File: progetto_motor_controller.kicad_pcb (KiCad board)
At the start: 4 copper layers, 55 parts, among them J1 USB_B_Micro, J2 Screw_Terminal_01x02, J3 SWD, J4 Screw_Terminal_01x03, Q1 AO3401A, SW1 SW_SPDT, U1 STM32F103C8Tx, U2 LMR504010-Q1, U3 USBLC6-2P6, U4 L6234PD, U5 INA240A2D, U6 INA240A2D, Y1 16MHz

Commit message: Third commit
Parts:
- removed C10: 10n, Capacitor_SMD:C_0402_1005Metric
- removed C11: 100 nF, Capacitor_SMD:C_0603_1608Metric
- removed C12: 10 uF, Capacitor_SMD:C_1206_3216Metric
- removed C13, C15: 0.1uF, Capacitor_SMD:C_0402_1005Metric
- removed C14: 220nF, Capacitor_SMD:C_0402_1005Metric
- removed C18: 100nF, Capacitor_SMD:C_0603_1608Metric
- removed C19: 100uF, Capacitor_SMD:CP_Elec_6.3x5.8
- removed D4, D5: IN4148, Diode_SMD:D_SOD-323F
- removed F1: 500mA, Fuse:Fuse_0603_1608Metric
- removed J2: Screw_Terminal_01x02, TerminalBlock_Phoenix:TerminalBlock_Phoenix_PT-1,5-2-3.5-H_1x02_P3.50mm_Horizontal
- removed J3: SWD, Connector_PinSocket_1.27mm:PinSocket_2x05_P1.27mm_Vertical_SMD
- removed L1: 39n, Inductor_SMD:L_0402_1005Metric
- removed L2: 10 uH, Inductor_SMD:L_Sunlord_MWSA0518_5.4x5.2mm
- removed Q1: AO3401A, Package_TO_SOT_SMD:SOT-23
- removed R10, R9: 2m, Resistor_SMD:R_Shunt_Ohmite_LVK12
- removed U5, U6: INA240A2D, Package_SO:TSSOP-8_4.4x3mm_P0.65mm
- added J8: Screw_Terminal_01x02, TerminalBlock_Phoenix:TerminalBlock_Phoenix_PT-1,5-2-3.5-H_1x02_P3.50mm_Horizontal, F.Cu at (175.5, 98.9)
- added Q8: AO3401A, Package_TO_SOT_SMD:SOT-23, F.Cu at (184.2, 97.0)
- added U7: MYRGC07506_1, MyLibrary:Murata_picoBK, F.Cu at (133.2, 66.4)
- added U8: TLV707, MyLibrary:TLV707, F.Cu at (157.6, 90.3)
- C16: value 10nF -> 0.1uF; moved to F.Cu
- C17: value 1uF -> 0.1uF; footprint Capacitor_SMD:C_0603_1608Metric -> Capacitor_SMD:C_0402_1005Metric; moved to F.Cu
- C6: value 10u -> 100n; footprint Capacitor_SMD:C_1206_3216Metric -> Capacitor_SMD:C_0402_1005Metric
- C8: value 1u -> 2u2
- D1, D3: value B5819W -> LED_Small; footprint Diode_SMD:D_SOD-123 -> LED_SMD:LED_0603_1608Metric
- J4: moved to F.Cu
- R5: value 100k -> 1k5
- R6: value 33k -> 1k5
- R7: footprint Resistor_SMD:R_0603_1608Metric -> Resistor_SMD:R_0402_1005Metric
- R8: value 4.7K -> 10k; moved to F.Cu
- U1: value STM32F103C8Tx -> STM32F303RETx; footprint Package_QFP:LQFP-48_7x7mm_P0.5mm -> Package_QFP:LQFP-64_10x10mm_P0.5mm
- U2: value LMR504010-Q1 -> SN65HVD253D; footprint Package_TO_SOT_SMD:TSOT-23-6_HandSoldering -> Package_SO:SOIC-8_3.9x4.9mm_P1.27mm
- U4: value L6234PD -> TMC6140; footprint Package_TO_SOT_SMD:L6234PD -> MyLibrary:TMC6140-LA; moved to F.Cu
- moved J4 58.3 mm to (124.9, 118.2), turned to 0 degrees
- moved U2 57.1 mm to (102.4, 78.6), turned to 0 degrees
- moved C17 48.1 mm to (174.2, 79.3), turned to 0 degrees
- moved C16 45.4 mm to (174.2, 81.2), turned to 0 degrees
- moved U4 41.3 mm to (107.8, 112.0), turned to 180 degrees
- moved D2 38.1 mm to (163.2, 64.4), turned to 0 degrees
- moved C5 36.8 mm to (112.6, 95.6), turned to 0 degrees
- moved U3 36.4 mm to (119.1, 78.0)
- moved J1 35.2 mm to (119.1, 72.7)
- moved H2 34.4 mm to (134.1, 94.4)
- moved SW1 33.9 mm to (156.8, 81.3), turned to 0 degrees
- moved H4 33.4 mm to (144.2, 93.5)
- moved R4 31.7 mm to (132.3, 108.1), turned to 0 degrees
- moved R3 30.4 mm to (158.6, 67.3)
- moved Y1 30.1 mm to (154.5, 65.3), turned to 0 degrees
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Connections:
- net Net-(U1-Pad16) renamed BOARD_TEMP
- net Net-(U1-Pad38) renamed ENC_B
- C1 pad 1: +3V3 -> 3V3_MCU
- C16 pad 1: Net-(C16-Pad1) -> 3V3_VDAA
- C16 pad 2: Net-(C16-Pad2) -> GND
- C17 pad 1: Net-(C17-Pad1) -> 3V3_VDAA
- C2 pad 1: +3V3 -> 3V3_MCU
- C3 pad 1: +3V3 -> 3V3_MCU
- C4 pad 1: +3V3 -> 3V3_MCU
- C5 pad 1: +3V3 -> 3V3_MCU
- C6 pad 1: BUCK_IN -> 3V3_MCU
- C8 pad 1: +3.3VA -> 5V
- D1 pad 2: +5V -> LED_R
- D2 pad 2: LED_STATUS -> LED_G
- D3 pad 1: BUCK_SW -> Net-(D3-Pad1)
- D3 pad 2: GND -> LED_B
- FB1 pad 1: BUCK_IN -> VDD
- FB1 pad 2: Net-(D1-Pad1) -> Net-(FB1-Pad2)
- J1 pad 1: +5V -> 5V
- J1 pad 4: Net-(J1-Pad4) -> unconnected-(J1-Pad4)
- J1 pad 6: Net-(J1-Pad6) -> unconnected-(J1-Pad6)
- R2 pad 1: Net-(D2-Pad1) -> Net-(D1-Pad1)
- R4 pad 1: Net-(J3-Pad2) -> SWDIO
- R4 pad 2: SWDIO -> Net-(J2-Pad4)
- R5 pad 1: BUCK_IN -> Net-(D2-Pad1)
- R5 pad 2: BUCK_EN -> GND
- R6 pad 1: +3V3 -> Net-(D3-Pad1)
- R6 pad 2: BUCK_FB -> GND
- R7 pad 1: BUCK_FB -> FAN_PWM
- R7 pad 2: GND -> Net-(Q1-Pad2)
- R8 pad 1: L6234_EN -> GND
- R8 pad 2: GND -> Net-(Q1-Pad2)
- SW1 pad 1: +3V3 -> 3V3_MCU
- U1 pad 1: +3V3 -> 3V3_MCU
- U1 pad 10: C1_SENSE -> PWM_HC
- U1 pad 11: C2_SENSE -> unconnected-(U1-Pad11)
- U1 pad 12: Net-(U1-Pad12) -> GND
- U1 pad 13: Net-(U1-Pad13) -> 3V3_VDAA
- U1 pad 14: Net-(U1-Pad14) -> FAN_PWM
- U1 pad 15: Net-(U1-Pad15) -> unconnected-(U1-Pad15)
- U1 pad 17: Net-(U1-Pad17) -> C1_SENSE
- U1 pad 18: Net-(U1-Pad18) -> GND
- U1 pad 19: Net-(U1-Pad19) -> 3V3_MCU
- U1 pad 2: Net-(U1-Pad2) -> unconnected-(U1-Pad2)
- U1 pad 20: Net-(U1-Pad20) -> C2_SENSE
- U1 pad 21: Net-(U1-Pad21) -> unconnected-(U1-Pad21)
- U1 pad 22: Net-(U1-Pad22) -> unconnected-(U1-Pad22)
- U1 pad 23: GND -> PWM_LA
- U1 pad 24: +3V3 -> unconnected-(U1-Pad24)
- U1 pad 25: Net-(U1-Pad25) -> unconnected-(U1-Pad25)
- U1 pad 26: Net-(U1-Pad26) -> PWM_LB
- U1 pad 27: Net-(U1-Pad27) -> PWM_LC
- U1 pad 28: Net-(U1-Pad28) -> ENABLE
- U1 pad 29: PH_A_PWM -> SH_SET
- U1 pad 3: Net-(U1-Pad3) -> unconnected-(U1-Pad3)
- U1 pad 30: PH_B_PWM -> DIAG
- U1 pad 31: PH_C_PWM -> GND
- U1 pad 32: USB_D- -> 3V3_MCU
- U1 pad 33: USB_D+ -> V_EMF_SENSE_C
- U1 pad 34: SWDIO -> unconnected-(U1-Pad34)
- U1 pad 35: GND -> V_EMF_SENSE_B
- U1 pad 36: +3V3 -> V_EMF_SENSE_A
- U1 pad 37: SWCLK -> ENC_A
- U1 pad 39: SWO -> ENC_I
- U1 pad 4: Net-(U1-Pad4) -> unconnected-(U1-Pad4)
- U1 pad 40: Net-(U1-Pad40) -> LED_R
- U1 pad 41: Net-(U1-Pad41) -> LED_G
- U1 pad 42: Net-(U1-Pad42) -> LED_B
- U1 pad 43: L6234_EN -> unconnected-(U1-Pad43)
- U1 pad 44: BOOT0 -> USB_D-
- U1 pad 45: Net-(U1-Pad45) -> USB_D+
- U1 pad 46: LED_STATUS -> SWDIO
- U1 pad 48: +3V3 -> 3V3_MCU
- U1 pad 8: GND -> PWM_HA
- U1 pad 9: +3.3VA -> PWM_HB
- U2 pad 1: BUCK_BST -> CAN_TX
- U2 pad 3: BUCK_FB -> 5V
- U2 pad 4: BUCK_EN -> CAN_RX
- U2 pad 5: BUCK_IN -> GND
- U2 pad 6: BUCK_SW -> CAN_L
- U3 pad 5: +5V -> 5V
- U4 pad 1: GND -> LC
- U4 pad 10: GND -> Net-(68u1-Pad2)
- U4 pad 11: GND -> VDD
- U4 pad 12: +48V -> Net-(C11-Pad1)
- U4 pad 13: L6234_EN -> PWM_HA
- U4 pad 14: PH_C_PWM -> PWM_LA
- U4 pad 15: PH_C -> PWM_HB
- U4 pad 16: Net-(C17-Pad1) -> PWM_LB
- U4 pad 17: Net-(C16-Pad2) -> PWM_HC
- U4 pad 18: Net-(C14-Pad1) -> PWM_LC
- U4 pad 19: GND -> SH_SET
- U4 pad 2: GND -> Net-(C14-Pad2)
- U4 pad 20: GND -> DIAG
- U4 pad 3: L6234_EN -> HB
- U4 pad 4: PH_B_PWM -> PH_B_CS
- U4 pad 5: PH_B_CS -> LB
- U4 pad 6: PH_A_CS -> LA
- U4 pad 7: PH_A_PWM -> PH_A_CS
- U4 pad 8: L6234_EN -> HA
- U4 pad 9: +48V -> Net-(C13-Pad2)
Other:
- copper layers 4 -> 2
- net class Default removed

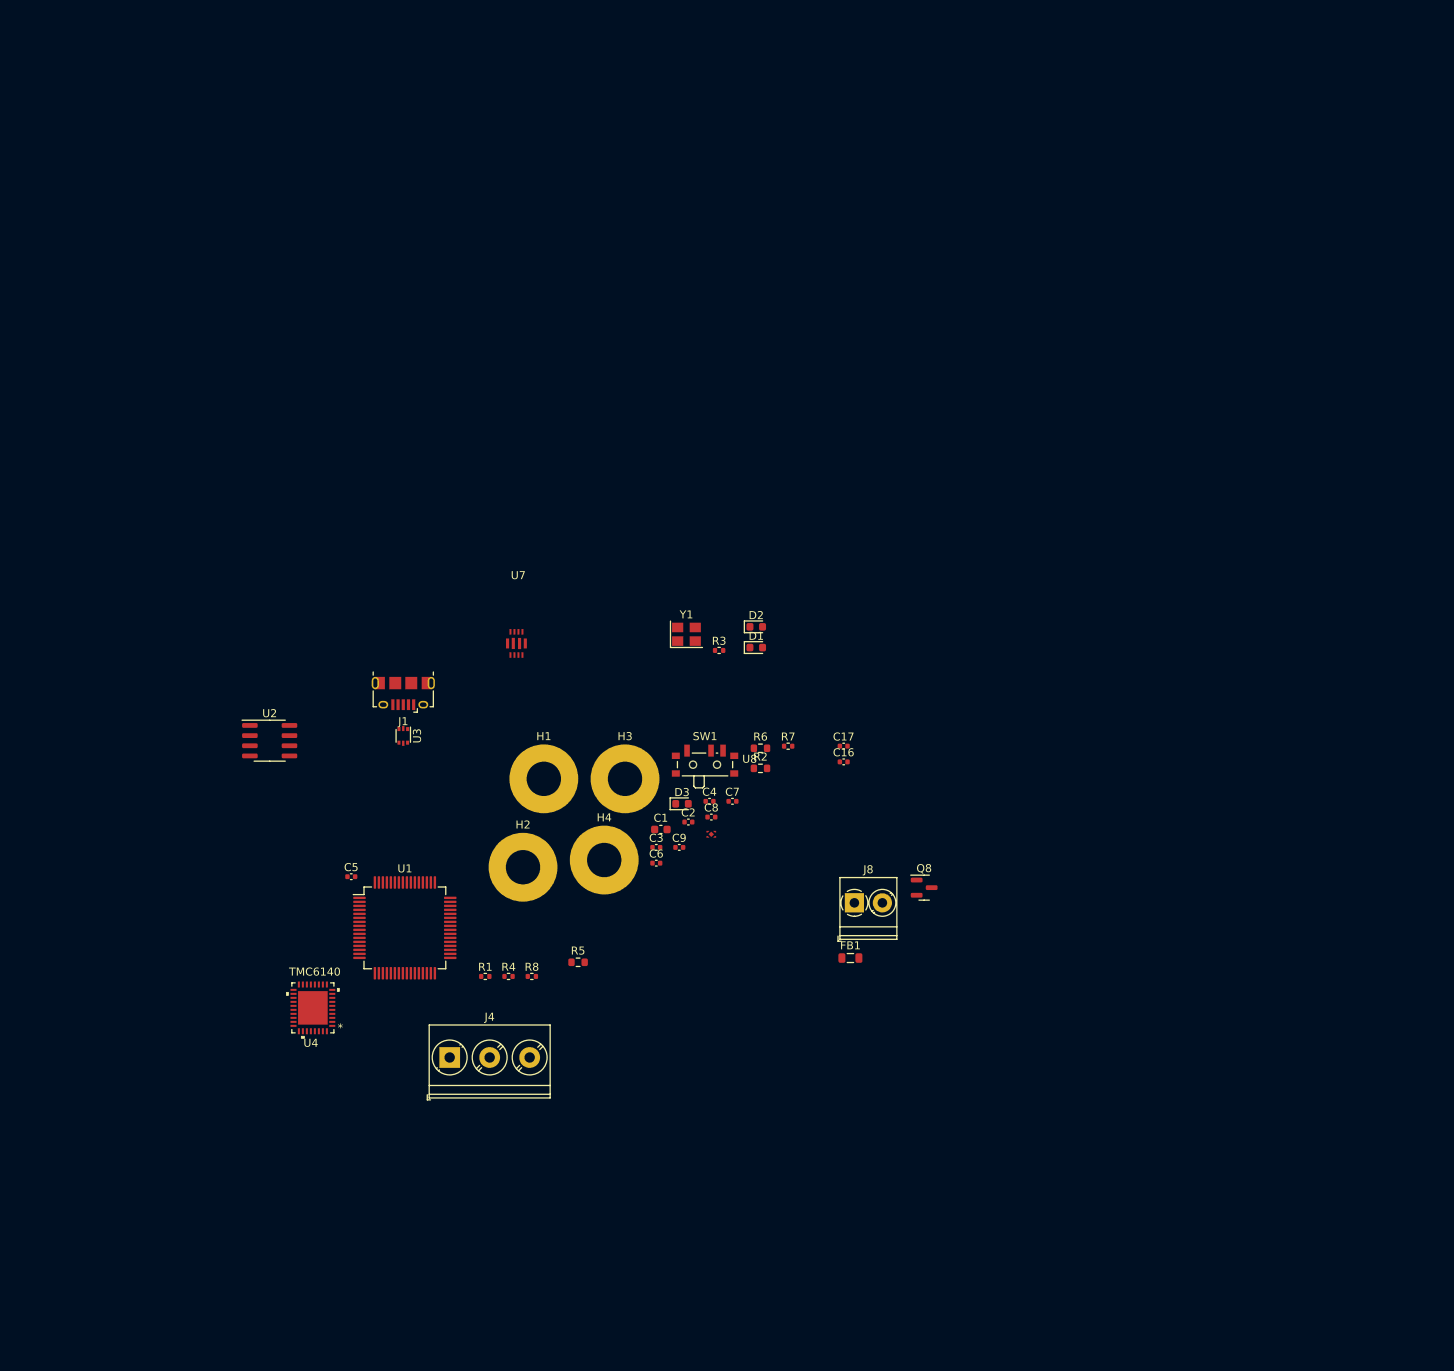
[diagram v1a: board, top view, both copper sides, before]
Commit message: added footprints
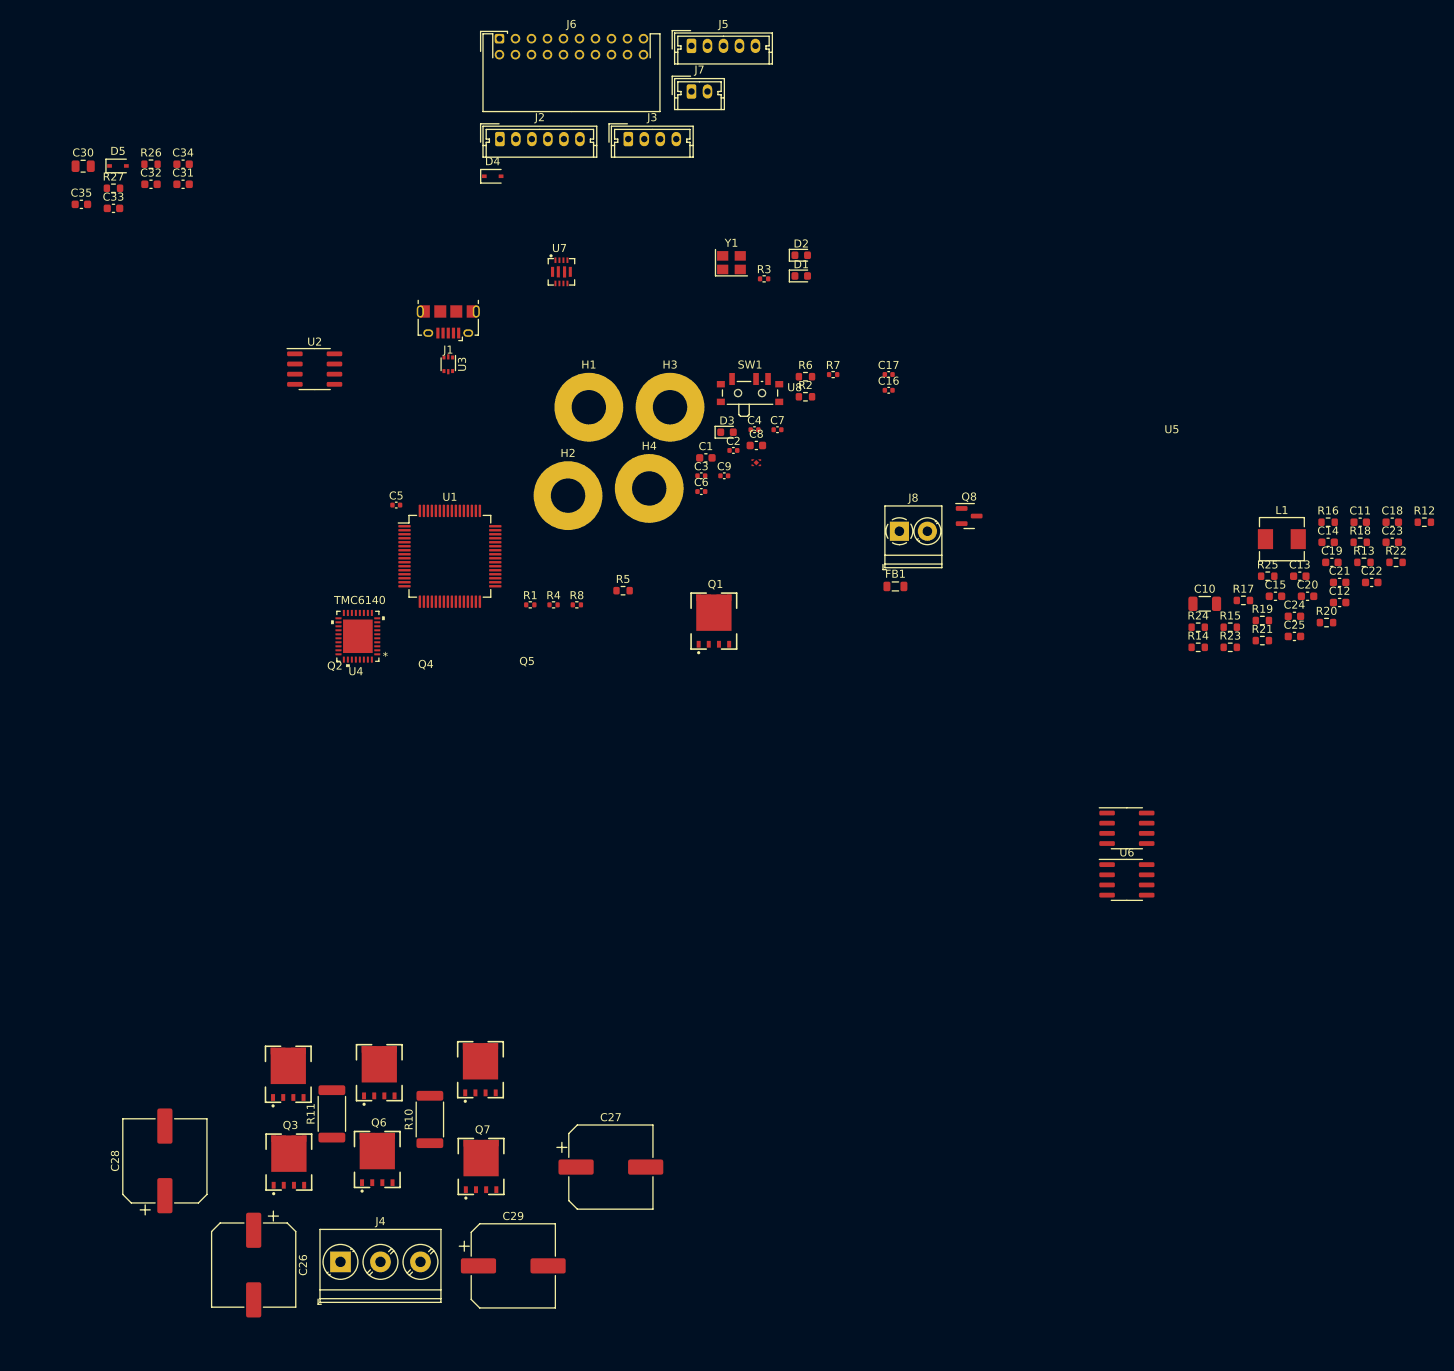
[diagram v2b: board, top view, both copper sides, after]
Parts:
- added C10: 47u, Capacitor_SMD:C_1206_3216Metric, F.Cu at (219.3, 61.5)
- added C11: 100n, Capacitor_SMD:C_0603_1608Metric, F.Cu at (238.7, 51.3)
- added C12: 10u, Capacitor_SMD:C_0603_1608Metric, F.Cu at (236.1, 61.3)
- added C13: 680n, Capacitor_SMD:C_0603_1608Metric, F.Cu at (231.2, 58.0)
- added C14: 680n, Capacitor_SMD:C_0603_1608Metric, F.Cu at (234.7, 53.8)
- added C15: 680n, Capacitor_SMD:C_0603_1608Metric, F.Cu at (228.1, 60.5)
- added C18: ns, Capacitor_SMD:C_0603_1608Metric, F.Cu at (242.7, 51.3)
- added C19: ns, Capacitor_SMD:C_0603_1608Metric, F.Cu at (235.2, 56.3)
- added C20: 10u, Capacitor_SMD:C_0603_1608Metric, F.Cu at (232.1, 60.5)
- added C21: 1n, Capacitor_SMD:C_0603_1608Metric, F.Cu at (236.1, 58.8)
- added C22: 1n, Capacitor_SMD:C_0603_1608Metric, F.Cu at (240.2, 58.8)
- added C23: 10u, Capacitor_SMD:C_0603_1608Metric, F.Cu at (242.7, 53.8)
- added C24: 1n, Capacitor_SMD:C_0603_1608Metric, F.Cu at (230.5, 63.1)
- added C25: 10u, Capacitor_SMD:C_0603_1608Metric, F.Cu at (230.5, 65.6)
- added C26: 680u, Capacitor_SMD:CP_Elec_10x12.6, F.Cu at (100.4, 144.2)
- added C27: 680u, Capacitor_SMD:CP_Elec_10x12.6, F.Cu at (145.1, 131.9)
- added C28: 680u, Capacitor_SMD:CP_Elec_10x12.6, F.Cu at (89.3, 131.1)
- added C29: 680u, Capacitor_SMD:CP_Elec_10x12.6, F.Cu at (132.8, 144.2)
- added C30: 22u, Capacitor_SMD:C_0805_2012Metric, F.Cu at (79.1, 6.79)
- added C31: 1u, Capacitor_SMD:C_0603_1608Metric, F.Cu at (91.6, 9.05)
- added C32: 1u, Capacitor_SMD:C_0603_1608Metric, F.Cu at (87.6, 9.05)
- added C33: 15p, Capacitor_SMD:C_0603_1608Metric, F.Cu at (82.9, 12.1)
- added C34: 22u, Capacitor_SMD:C_0603_1608Metric, F.Cu at (91.6, 6.54)
- added C35: nc, Capacitor_SMD:C_0603_1608Metric, F.Cu at (78.9, 11.6)
- added D4: D_Small, Diode_SMD:D_SOD-323, F.Cu at (130.3, 8.05)
- added D5: D_TVS, Diode_SMD:D_SOD-323, F.Cu at (83.4, 6.76)
- added J2: Conn_01x06, Connector_Molex:Molex_Micro-Latch_53253-0670_1x06_P2.00mm_Vertical, F.Cu at (131.2, 3.40)
- added J3: Conn_01x04, Connector_Molex:Molex_Micro-Latch_53253-0470_1x04_P2.00mm_Vertical, F.Cu at (147.2, 3.40)
- added J5: Conn_01x05, Connector_Molex:Molex_Micro-Latch_53253-0570_1x05_P2.00mm_Vertical, F.Cu at (155.1, -8.25)
- added J6: Conn_02x10_Counter_Clockwise, Connector_JST:JST_PHD_S20B-PHDSS_2x10_P2.00mm_Horizontal, F.Cu at (131.1, -9.15)
- added J7: Conn_01x02, Connector_Molex:Molex_Micro-Latch_53253-0270_1x02_P2.00mm_Vertical, F.Cu at (155.1, -2.55)
- added L1: 68u, Inductor_SMD:L_Sunlord_MWSA0518_5.4x5.2mm, F.Cu at (228.9, 53.4)
- added Q1: BSC022N04LSATMA1, MyLibrary:TDSON-8-6, F.Cu at (157.9, 63.6)
- added Q2: BSC022N04LSATMA1, MyLibrary:TDSON-8-6, F.Cu at (104.7, 120.3)
- added Q3: BSC022N04LSATMA1, MyLibrary:TDSON-8-6, F.Cu at (104.8, 131.3)
- added Q4: BSC022N04LSATMA1, MyLibrary:TDSON-8-6, F.Cu at (116.1, 120.1)
- added Q5: BSC022N04LSATMA1, MyLibrary:TDSON-8-6, F.Cu at (128.8, 119.7)
- added Q6: BSC022N04LSATMA1, MyLibrary:TDSON-8-6, F.Cu at (115.8, 130.9)
- added Q7: BSC022N04LSATMA1, MyLibrary:TDSON-8-6, F.Cu at (128.8, 131.8)
- added R10: 2m, Resistor_SMD:R_2512_6332Metric, F.Cu at (122.4, 126.0)
- added R11: 2m, Resistor_SMD:R_2512_6332Metric, F.Cu at (110.2, 125.2)
- added R12: 0R, Resistor_SMD:R_0603_1608Metric, F.Cu at (246.7, 51.3)
- added R13: 0R, Resistor_SMD:R_0603_1608Metric, F.Cu at (239.2, 56.3)
- added R14: 10, Resistor_SMD:R_0603_1608Metric, F.Cu at (218.5, 66.9)
- added R15: 10, Resistor_SMD:R_0603_1608Metric, F.Cu at (222.5, 64.4)
- added R16: 10, Resistor_SMD:R_0603_1608Metric, F.Cu at (234.7, 51.3)
- added R17: 10, Resistor_SMD:R_0603_1608Metric, F.Cu at (224.1, 61.1)
- added R18: 33k, Resistor_SMD:R_0603_1608Metric, F.Cu at (238.7, 53.8)
- added R19: 33k, Resistor_SMD:R_0603_1608Metric, F.Cu at (226.5, 63.6)
- added R20: 33k, Resistor_SMD:R_0603_1608Metric, F.Cu at (234.5, 63.8)
- added R21: 3k9, Resistor_SMD:R_0603_1608Metric, F.Cu at (226.5, 66.1)
- added R22: 3k9, Resistor_SMD:R_0603_1608Metric, F.Cu at (243.2, 56.3)
- added R23: 3k9, Resistor_SMD:R_0603_1608Metric, F.Cu at (222.5, 66.9)
- added R24: 10, Resistor_SMD:R_0603_1608Metric, F.Cu at (218.5, 64.4)
- added R25: 10, Resistor_SMD:R_0603_1608Metric, F.Cu at (227.2, 58.0)
- added R26: 680k, Resistor_SMD:R_0603_1608Metric, F.Cu at (87.6, 6.54)
- added R27: 120k, Resistor_SMD:R_0603_1608Metric, F.Cu at (82.9, 9.55)
- added U5: TSC2011, Package_SO:SOIC-8_3.9x4.9mm_P1.27mm, F.Cu at (209.6, 89.5)
- added U6: TSC2011, Package_SO:SOIC-8_3.9x4.9mm_P1.27mm, F.Cu at (209.6, 96.0)
- C8: footprint Capacitor_SMD:C_0402_1005Metric -> Capacitor_SMD:C_0603_1608Metric
- moved C4 46.8 mm to (163.0, 39.7)
- moved C7 46.8 mm to (165.9, 39.7)
- moved C1 46.8 mm to (156.9, 43.2)
- moved C16 46.8 mm to (179.8, 34.8)
- moved C17 46.8 mm to (179.8, 32.8)
- moved C8 46.8 mm to (163.2, 41.7)
- moved D2 46.8 mm to (168.8, 17.9)
- moved H1 46.8 mm to (142.3, 36.9)
- moved H2 46.8 mm to (139.7, 48.0)
- moved H3 46.8 mm to (152.4, 36.9)
- moved J1 46.8 mm to (124.7, 26.2)
- moved J8 46.8 mm to (181.1, 52.4)
- moved R2 46.8 mm to (169.4, 35.6)
- moved R7 46.8 mm to (172.8, 32.8)
- moved U1 46.8 mm to (124.9, 55.5)
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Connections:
- U4 pad 2: Net-(C14-Pad2) -> /Inverter/CV
- U4 pad 34: Net-(C15-Pad2) -> /Inverter/CW
- U4 pad 9: Net-(C13-Pad2) -> /Inverter/CU

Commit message: fourth commit
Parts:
- Q1, Q2, Q3, Q4, Q5, Q6, Q7: footprint MyLibrary:TDSON-8-6 -> MyLibrary:TDSON-8-6_copy
- moved C14 153.3 mm to (86.5, 93.1)
- moved C19 153.3 mm to (87.0, 95.6)
- moved R12 153.3 mm to (98.5, 90.6)
- moved R16 153.3 mm to (86.5, 90.6)
- moved C11 153.3 mm to (90.5, 90.6)
- moved C21 153.3 mm to (87.9, 98.1)
- moved C22 153.3 mm to (91.9, 98.1)
- moved R13 153.3 mm to (91.0, 95.6)
- moved R18 153.3 mm to (90.5, 93.1)
- moved C18 153.3 mm to (94.5, 90.6)
- moved C23 153.3 mm to (94.5, 93.1)
- moved R22 153.3 mm to (95.0, 95.6)
- moved J7 139.0 mm to (76.7, 112.2), turned to -90 degrees
- moved L1 128.3 mm to (113.7, 109.8)
- moved J5 124.8 mm to (150.2, 116.5), turned to 90 degrees
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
